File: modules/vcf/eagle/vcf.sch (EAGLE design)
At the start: 78 parts, among them IC1 TL074P, IC2 LM13700N, IC3 TL074P, Q1 2N3906, Q2 2N3906, X1 22-23-2031, X10 AUDIO INPUTS, X11 POWER, X12 FILTER OUT, X2 CV INPUTS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

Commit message: Badly finish VCF board layout (single)
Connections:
- net N$1 renamed N$1V-OCT
- net N$31 renamed N$LP-OUT
- net N$40 renamed N$BP-OUT
- net N$51 renamed N$HP-OUT
- removed net N$6: X10-2.KL, X7-2.S
- new net N$1: X10-1.KL, X7-2.S
- net N$16: now also X10-2.KL; no longer X10-1.KL
- net N$37: now also IC3D.-IN; no longer IC3A.-IN
- net N$47: now also IC3D.OUT; no longer IC3A.OUT
- net N$49: now also IC3A.-IN; no longer IC3D.-IN
- net N$50: now also IC3A.OUT; no longer IC3D.OUT
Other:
- moved on the sheet: IC3A, IC3D
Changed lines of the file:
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@@
 <?xml version="1.0" encoding="utf-8"?>
 <!DOCTYPE eagle SYSTEM "eagle.dtd">
-<eagle version="7.5.0">
+<eagle version="7.3.0">
 <drawing>
 <settings>
@@
 <instance part="IC1" gate="C" x="119.38" y="170.18" rot="MR180"/>
 <instance part="IC1" gate="D" x="76.2" y="233.68" rot="MR180"/>
-<instance part="IC3" gate="A" x="299.72" y="104.14" rot="MR180"/>
+<instance part="IC3" gate="A" x="325.12" y="53.34" rot="MR180"/>
 <instance part="IC3" gate="B" x="119.38" y="53.34" rot="MR180"/>
 <instance part="IC3" gate="C" x="220.98" y="53.34" rot="MR180"/>
-<instance part="IC3" gate="D" x="325.12" y="53.34" rot="MR180"/>
+<instance part="IC3" gate="D" x="299.72" y="104.14" rot="MR180"/>
 <instance part="LED1" gate="G$1" x="99.06" y="76.2" rot="R180"/>
 <instance part="LED2" gate="G$1" x="104.14" y="78.74"/>
@@
 <wire x1="55.88" y1="38.1" x2="40.64" y2="38.1" width="0.1524" layer="91"/>
 <junction x="40.64" y="38.1"/>
+<junction x="55.88" y="38.1"/>
 </segment>
 </net>
@@
 </segment>
 <segment>
-<pinref part="IC3" gate="A" pin="+IN"/>
-<wire x1="292.1" y1="101.6" x2="289.56" y2="101.6" width="0.1524" layer="91"/>
 <pinref part="SUPPLY24" gate="GND" pin="GND"/>
 <wire x1="289.56" y1="101.6" x2="289.56" y2="99.06" width="0.1524" layer="91"/>
+<pinref part="IC3" gate="D" pin="+IN"/>
+<wire x1="292.1" y1="101.6" x2="289.56" y2="101.6" width="0.1524" layer="91"/>
 </segment>
 <segment>
@@
 <pinref part="SUPPLY26" gate="GND" pin="GND"/>
 <wire x1="314.96" y1="48.26" x2="314.96" y2="50.8" width="0.1524" layer="91"/>
-<wire x1="314.96" y1="50.8" x2="317.5" y2="50.8" width="0.1524" layer="91"/>
-<pinref part="IC3" gate="D" pin="+IN"/>
+<pinref part="IC3" gate="A" pin="+IN"/>
+<wire x1="317.5" y1="50.8" x2="314.96" y2="50.8" width="0.1524" layer="91"/>
 </segment>
 <segment>
@@
 <wire x1="55.88" y1="12.7" x2="40.64" y2="12.7" width="0.1524" layer="91"/>
 <junction x="40.64" y="12.7"/>
-</segment>
-</net>
-<net name="N$1" class="0">
+<junction x="55.88" y="12.7"/>
+</segment>
+</net>
+<net name="N$1V-OCT" class="0">
 <segment>
 <pinref part="X2" gate="-1" pin="KL"/>
@@
 </segment>
 </net>
-<net name="N$6" class="0">
-<segment>
-<wire x1="45.72" y1="68.58" x2="45.72" y2="119.38" width="0.1524" layer="91"/>
-<pinref part="X7" gate="-2" pin="S"/>
-<wire x1="45.72" y1="119.38" x2="38.1" y2="119.38" width="0.1524" layer="91"/>
-<pinref part="X10" gate="-2" pin="KL"/>
-<wire x1="38.1" y1="68.58" x2="45.72" y2="68.58" width="0.1524" layer="91"/>
-</segment>
-</net>
 <net name="N$16" class="0">
 <segment>
 <pinref part="X9" gate="-2" pin="S"/>
 <wire x1="43.18" y1="88.9" x2="38.1" y2="88.9" width="0.1524" layer="91"/>
-<pinref part="X10" gate="-1" pin="KL"/>
-<wire x1="38.1" y1="73.66" x2="43.18" y2="73.66" width="0.1524" layer="91"/>
-<wire x1="43.18" y1="73.66" x2="43.18" y2="88.9" width="0.1524" layer="91"/>
+<pinref part="X10" gate="-2" pin="KL"/>
+<wire x1="38.1" y1="68.58" x2="43.18" y2="68.58" width="0.1524" layer="91"/>
+<wire x1="43.18" y1="88.9" x2="43.18" y2="68.58" width="0.1524" layer="91"/>
 </segment>
 </net>
@@
 <wire x1="297.18" y1="114.3" x2="289.56" y2="114.3" width="0.1524" layer="91"/>
 <wire x1="289.56" y1="114.3" x2="289.56" y2="106.68" width="0.1524" layer="91"/>
-<pinref part="IC3" gate="A" pin="-IN"/>
+<pinref part="IC3" gate="D" pin="-IN"/>
 <wire x1="292.1" y1="106.68" x2="289.56" y2="106.68" width="0.1524" layer="91"/>
 <junction x="289.56" y="106.68"/>
@@
 <segment>
 <pinref part="R37" gate="G$1" pin="2"/>
-<wire x1="309.88" y1="104.14" x2="309.88" y2="99.06" width="0.1524" layer="91"/>
 <pinref part="C15" gate="G$1" pin="2"/>
 <wire x1="304.8" y1="114.3" x2="309.88" y2="114.3" width="0.1524" layer="91"/>
@@
 <junction x="309.88" y="114.3"/>
 <wire x1="309.88" y1="114.3" x2="309.88" y2="104.14" width="0.1524" layer="91"/>
-<pinref part="IC3" gate="A" pin="OUT"/>
+<pinref part="IC3" gate="D" pin="OUT"/>
+<wire x1="309.88" y1="104.14" x2="309.88" y2="99.06" width="0.1524" layer="91"/>
 <wire x1="307.34" y1="104.14" x2="309.88" y2="104.14" width="0.1524" layer="91"/>
 <junction x="309.88" y="104.14"/>
@@
 <wire x1="312.42" y1="55.88" x2="314.96" y2="55.88" width="0.1524" layer="91"/>
 <pinref part="C16" gate="G$1" pin="1"/>
-<wire x1="314.96" y1="55.88" x2="317.5" y2="55.88" width="0.1524" layer="91"/>
 <wire x1="320.04" y1="60.96" x2="314.96" y2="60.96" width="0.1524" layer="91"/>
 <junction x="314.96" y="60.96"/>
+<pinref part="IC3" gate="A" pin="-IN"/>
+<wire x1="317.5" y1="55.88" x2="314.96" y2="55.88" width="0.1524" layer="91"/>
 <junction x="314.96" y="55.88"/>
-<pinref part="IC3" gate="D" pin="-IN"/>
 </segment>
 </net>
@@
 <wire x1="335.28" y1="68.58" x2="335.28" y2="60.96" width="0.1524" layer="91"/>
 <wire x1="335.28" y1="60.96" x2="335.28" y2="53.34" width="0.1524" layer="91"/>
-<wire x1="335.28" y1="53.34" x2="332.74" y2="53.34" width="0.1524" layer="91"/>
 <pinref part="C16" gate="G$1" pin="2"/>
+<wire x1="335.28" y1="53.34" x2="335.28" y2="50.8" width="0.1524" layer="91"/>
 <wire x1="327.66" y1="60.96" x2="335.28" y2="60.96" width="0.1524" layer="91"/>
 <pinref part="R39" gate="G$1" pin="2"/>
-<wire x1="335.28" y1="50.8" x2="335.28" y2="53.34" width="0.1524" layer="91"/>
 <junction x="335.28" y="60.96"/>
+<pinref part="IC3" gate="A" pin="OUT"/>
+<wire x1="332.74" y1="53.34" x2="335.28" y2="53.34" width="0.1524" layer="91"/>
 <junction x="335.28" y="53.34"/>
-<pinref part="IC3" gate="D" pin="OUT"/>
-</segment>
-</net>
-<net name="N$31" class="0">
+</segment>
+</net>
+<net name="N$LP-OUT" class="0">
 <segment>
 <pinref part="R39" gate="G$1" pin="1"/>
@@
 </segment>
 </net>
-<net name="N$40" class="0">
+<net name="N$BP-OUT" class="0">
 <segment>
 <pinref part="X12" gate="-2" pin="KL"/>
@@
 </segment>
 </net>
-<net name="N$51" class="0">
+<net name="N$HP-OUT" class="0">
 <segment>
 <pinref part="X12" gate="-1" pin="KL"/>
@@
 </segment>
 </net>
+<net name="N$1" class="0">
+<segment>
+<pinref part="X10" gate="-1" pin="KL"/>
+<wire x1="38.1" y1="73.66" x2="45.72" y2="73.66" width="0.1524" layer="91"/>
+<pinref part="X7" gate="-2" pin="S"/>
+<wire x1="45.72" y1="73.66" x2="45.72" y2="119.38" width="0.1524" layer="91"/>
+<wire x1="45.72" y1="119.38" x2="38.1" y2="119.38" width="0.1524" layer="91"/>
+</segment>
+</net>
 </nets>
 </sheet>
 </sheets>
-<errors>
-</errors>
 </schematic>
 </drawing>

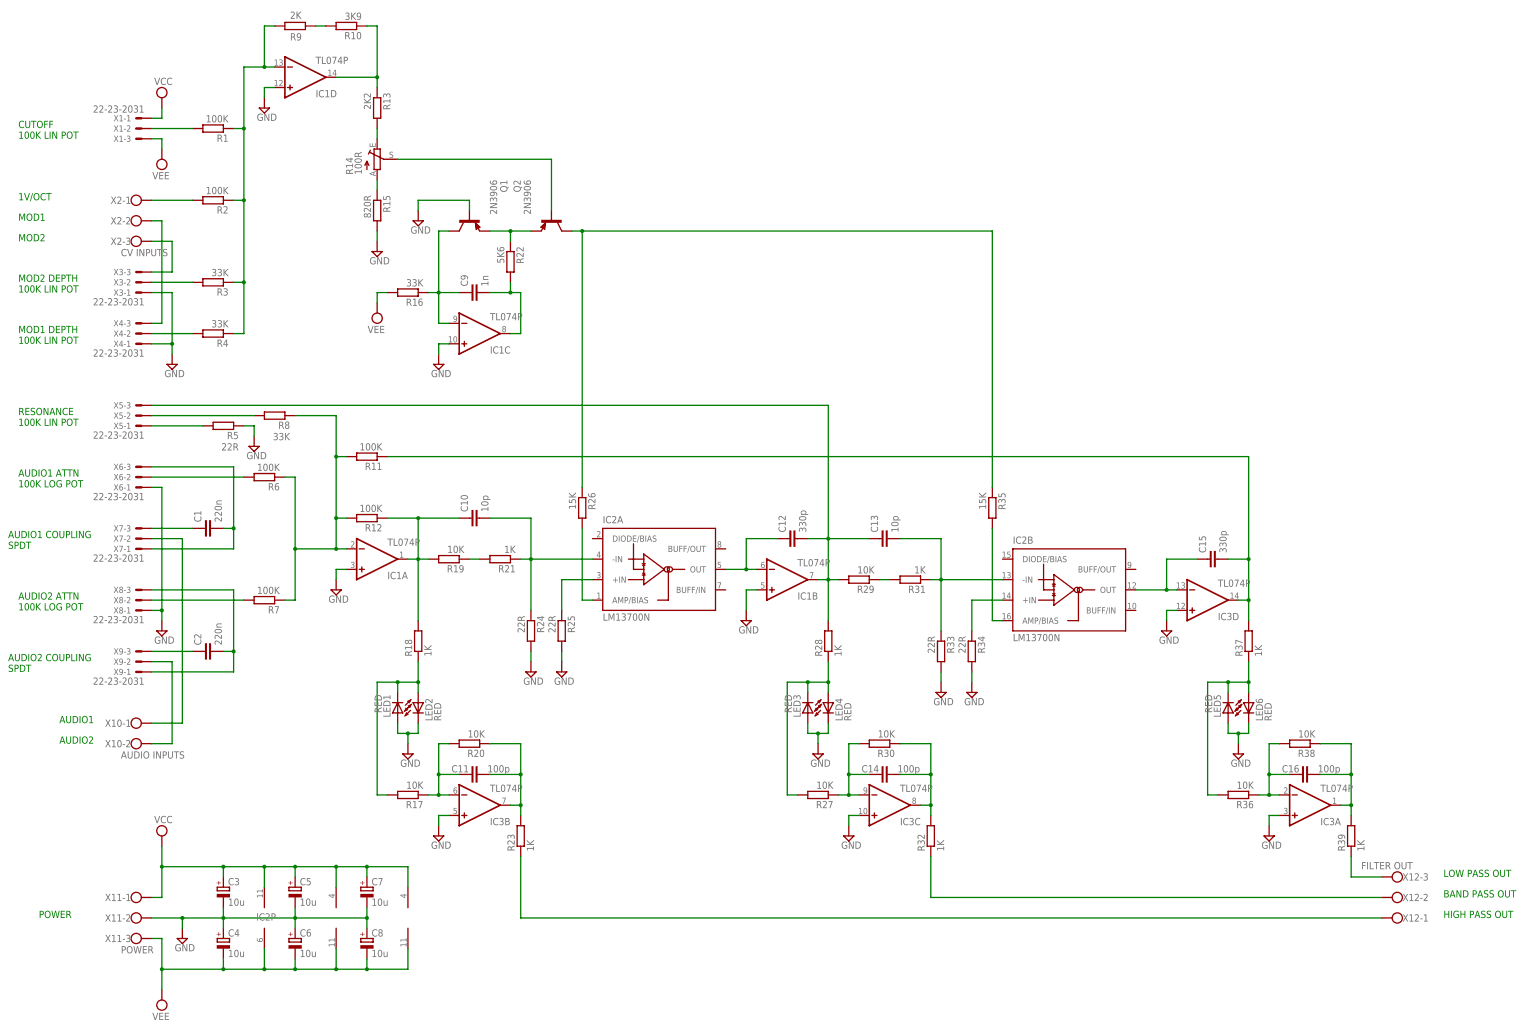
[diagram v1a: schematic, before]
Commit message: Redesign filter board without limitiers; double-sided
The single-sided board with limiters didn't work. The limiters
introduced DC offsets that made various opamps just max out, creating a
static DC output. The limiting circuitry is now removed, and the new PCB
design is a double-sided one because I could not be bothered making
another terrible single-sided one.
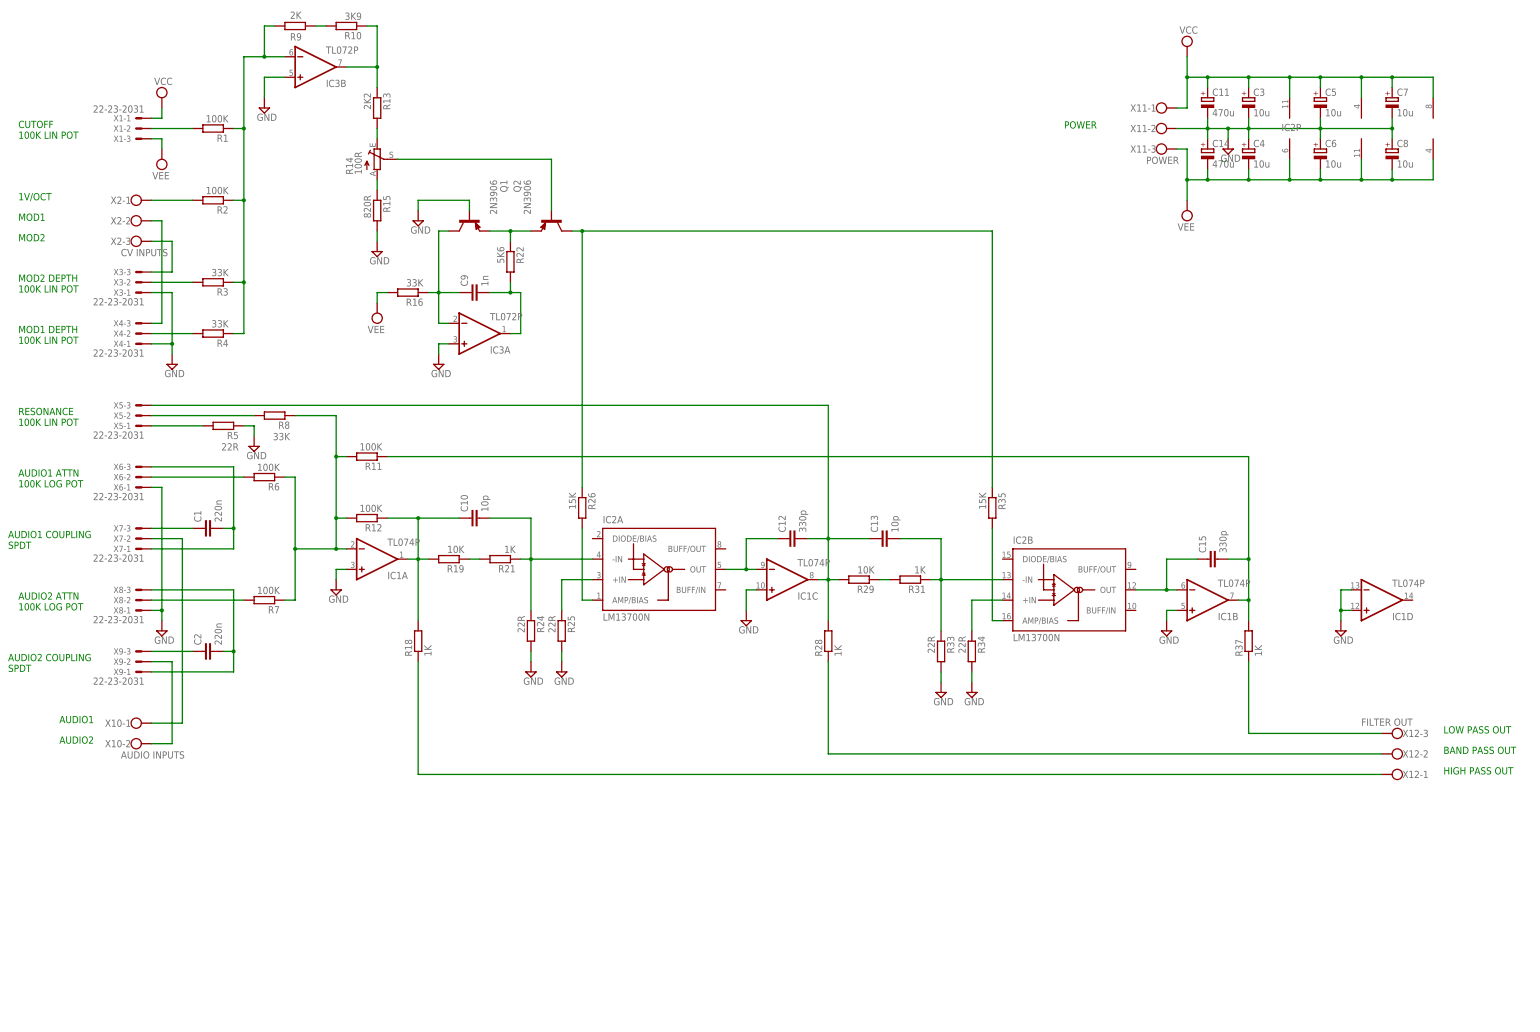
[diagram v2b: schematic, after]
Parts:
- removed C16: 100p, rcl:C-EU025-024X044
- removed LED1, LED2, LED3, LED4, LED5, LED6: RED, led:LED5MM
- removed R17, R20, R27, R30, R36, R38: 10K, rcl:R-EU_0204/7
- removed R23, R32, R39: 1K, rcl:R-EU_0204/7
- C11, C14: value 100p -> 470u; device rcl:C-EU025-024X044 -> rcl:CPOL-EUE2.5-6
- IC3: value TL074P -> TL072P; device linear:TL074P -> linear:TL072P
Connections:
- removed net N$41: LED1.C, LED2.A, R17.2, R18.1
- removed net N$42: LED3.C, LED4.A, R27.2, R28.1
- removed net N$43: C14.1, IC3C.-IN, R27.1, R30.2
- removed net N$44: C11.1, IC3B.-IN, R17.1, R20.2
- removed net N$45: C11.2, IC3B.OUT, R20.1, R23.2
- removed net N$46: C14.2, IC3C.OUT, R30.1, R32.2
- removed net N$48: LED5.C, LED6.A, R36.2, R37.1
- removed net N$49: C16.1, IC3A.-IN, R36.1, R38.2
- removed net N$50: C16.2, IC3A.OUT, R38.1, R39.2
- net GND: now also C11.-, C14.+, IC1D.-IN; no longer IC3C.+IN, IC3D.+IN, LED1.A, LED2.C, LED3.A, LED4.C, LED5.A, LED6.C
- net N$14: now also IC3A.OUT; no longer IC1C.OUT
- net N$15: now also IC3A.-IN; no longer IC1C.-IN
- net N$29: now also IC1C.-IN; no longer IC1B.-IN
- net N$37: now also IC1B.-IN; no longer IC3D.-IN
- net N$39: now also IC1C.OUT; no longer IC1B.OUT
- net N$47: now also IC1B.OUT; no longer IC3D.OUT
- net N$9: now also IC3B.OUT; no longer IC1D.OUT
- net N$BP-OUT: now also R28.1; no longer R32.1
- net N$EXP-CV: now also IC3B.-IN; no longer IC1D.-IN
- net N$HP-OUT: now also R18.1; no longer R23.1
- net N$LP-OUT: now also R37.1; no longer R39.1
- net VCC: now also C11.+
- net VEE: now also C14.-
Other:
- moved on the sheet: C3, C4, C5, C6, C7, C8, IC1B, IC1C, IC1D, IC2P, IC3A, IC3B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
